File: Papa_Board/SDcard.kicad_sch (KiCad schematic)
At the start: 12 parts, among them J8 693072010801, Q1 BSS138

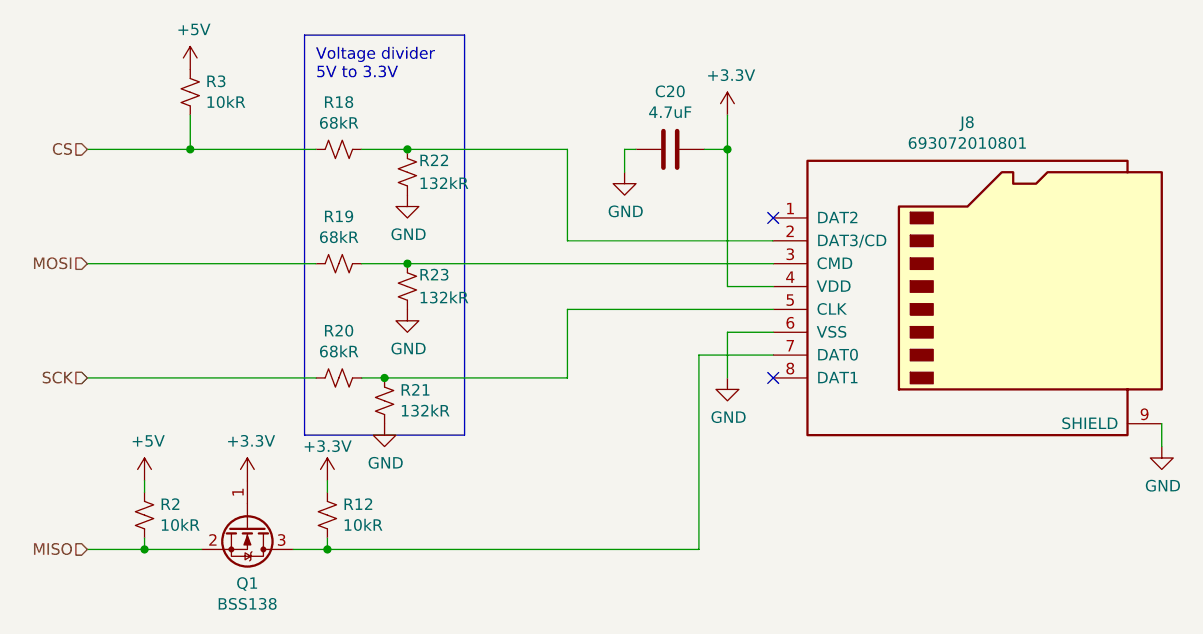
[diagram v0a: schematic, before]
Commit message: Remove level shifting + voltage dividers from SD card SPI lines
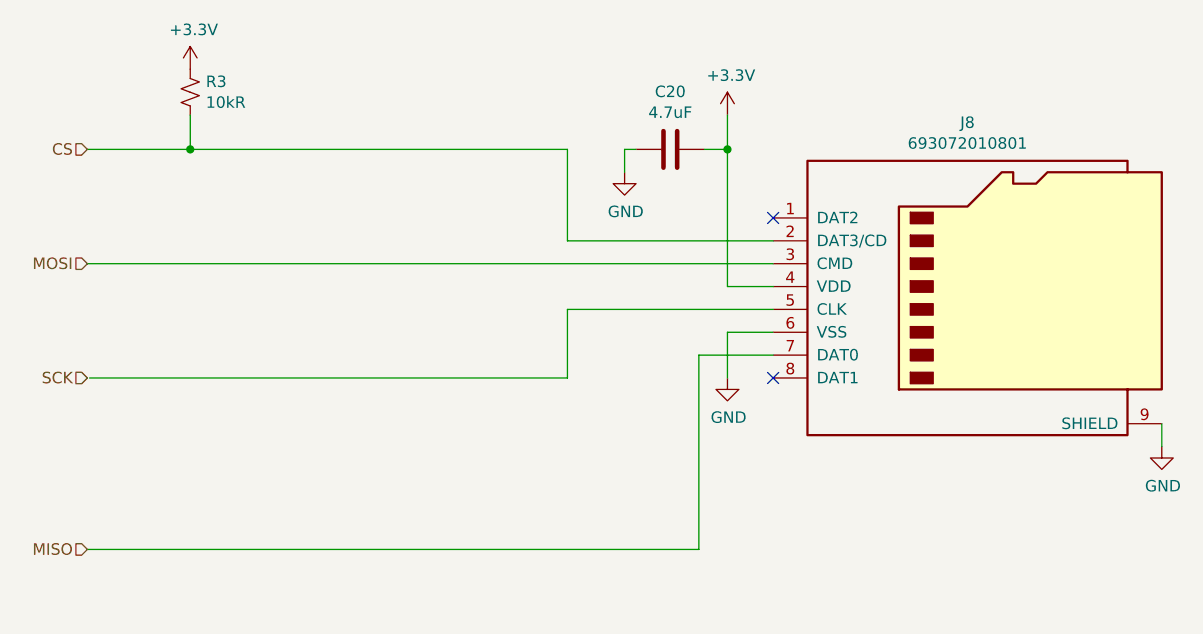
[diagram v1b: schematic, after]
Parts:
- removed Q1: BSS138, Package_TO_SOT_SMD:SOT-23, symbol Device:Q_NMOS_GSD
- removed R12, R2: 10kR, Resistor_SMD:R_0805_2012Metric_Pad1.20x1.40mm_HandSolder, symbol Device:R_Small_US
- removed R18: 68kR, Resistor_SMD:R_0805_2012Metric_Pad1.15x1.40mm_HandSolder, symbol Device:R_Small_US
- removed R19, R20: 68kR, Resistor_SMD:R_0805_2012Metric_Pad1.20x1.40mm_HandSolder, symbol Device:R_Small_US
- removed R21, R23: 132kR, Resistor_SMD:R_0805_2012Metric_Pad1.20x1.40mm_HandSolder, symbol Device:R_Small_US
- removed R22: 132kR, Resistor_SMD:R_0805_2012Metric_Pad1.15x1.40mm_HandSolder, symbol Device:R_Small_US
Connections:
- net +5V is gone; now on net +3V3: R3.1
- net CS: now also J8.2 (DAT3/CD)
- net MISO: now also J8.7 (DAT0)
- net MOSI: now also J8.3 (CMD)
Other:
- note removed: "Voltage divider 5V to 3.3V"

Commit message: Finish changes to PCB layout, clean up and simplify VCC layer
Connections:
- net SCK: now also J8.5 (CLK)
- net CS renamed CS_2
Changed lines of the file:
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@@
     (effects (font (size 1.27 1.27)) (justify right))
   )
-  (hierarchical_label "SCK" (shape input) (at 123.19 107.95 180)
+  (hierarchical_label "SCK" (shape input) (at 123.444 107.95 180)
     (effects (font (size 1.27 1.27)) (justify right))
   )
@@
     (effects (font (size 1.27 1.27)) (justify right))
   )
-  (hierarchical_label "CS" (shape input) (at 123.19 82.55 180)
+  (hierarchical_label "CS_2" (shape input) (at 123.19 82.55 180)
     (effects (font (size 1.27 1.27)) (justify right))
   )
@@
   (symbol (lib_id "power:+3.3V") (at 134.62 73.66 0) (unit 1)
     (in_bom yes) (on_board yes)
-    (property "Reference" "#PWR?" (id 0) (at 134.62 77.47 0)
+    (property "Reference" "#PWR0101" (id 0) (at 134.62 77.47 0)
       (effects (font (size 1.27 1.27)) hide)
     )

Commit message: Minor schematic/pcb adjustments
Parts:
- removed R3: 10kR, Resistor_SMD:R_0805_2012Metric_Pad1.15x1.40mm_HandSolder, symbol Device:R_Small_US
- added R12: 10kR, Resistor_SMD:R_0805_2012Metric_Pad1.20x1.40mm_HandSolder, symbol Device:R_Small_US
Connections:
- net +3V3: now also R12.1
- net CS_2: now also R12.2
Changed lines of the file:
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@@
     (pin "1")
-  )
-  (symbol (lib_id "Device:R_Small_US") (at 134.62 76.2 0) (unit 1)
-    (in_bom yes) (on_board yes)
-    (property "Reference" "R3" (id 0) (at 136.3472 75.0316 0)
-      (effects (font (size 1.27 1.27)) (justify left))
-    )
-    (property "Value" "10kR" (id 1) (at 136.3472 77.343 0)
-      (effects (font (size 1.27 1.27)) (justify left))
-    )
-    (property "Footprint" "Resistor_SMD:R_0805_2012Metric_Pad1.15x1.40mm_HandSolder" (id 2) (at 134.62 76.2 0)
-      (effects (font (size 1.27 1.27)) hide)
-    )
-    (property "Datasheet" "~" (id 3) (at 134.62 76.2 0)
-      (effects (font (size 1.27 1.27)) hide)
-    )
-    (pin "1")
-    (pin "2")
   )
   (symbol (lib_id "power:GND") (at 242.57 115.57 0) (unit 1)
@@
     (pin "1")
   )
+  (symbol (lib_id "Device:R_Small_US") (at 134.62 76.2 0) (unit 1)
+    (in_bom yes) (on_board yes)
+    (property "Reference" "R12" (id 0) (at 136.3472 75.0316 0)
+      (effects (font (size 1.27 1.27)) (justify left))
+    )
+    (property "Value" "10kR" (id 1) (at 136.3472 77.343 0)
+      (effects (font (size 1.27 1.27)) (justify left))
+    )
+    (property "Footprint" "Resistor_SMD:R_0805_2012Metric_Pad1.20x1.40mm_HandSolder" (id 2) (at 134.62 76.2 0)
+      (effects (font (size 1.27 1.27)) hide)
+    )
+    (property "Datasheet" "~" (id 3) (at 134.62 76.2 0)
+      (effects (font (size 1.27 1.27)) hide)
+    )
+    (pin "1")
+    (pin "2")
+  )
 )

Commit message: fixed volgtage logic levels, added test connectors and jumpers
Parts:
- added R21, R22, R23: 10kR, Resistor_SMD:R_0805_2012Metric_Pad1.20x1.40mm_HandSolder, symbol Device:R_Small_US
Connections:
- net +3V3: now also R21.1, R22.1, R23.1
- net MISO: now also R23.2
- net MOSI: now also R21.2
- net SCK: now also R22.2
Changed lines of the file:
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@@
 (kicad_sch (version 20211123) (generator eeschema)
   (paper "A4")
+  (junction (at 135.255 95.25) (diameter 0) (color 0 0 0 0)
+  )
+  (junction (at 135.255 107.95) (diameter 0) (color 0 0 0 0)
+  )
   (junction (at 194.31 82.55) (diameter 0) (color 0 0 0 0)
   )
   (junction (at 134.62 82.55) (diameter 0) (color 0 0 0 0)
+  )
+  (junction (at 135.89 127) (diameter 0) (color 0 0 0 0)
   )
   (no_connect (at 199.39 107.95))
@@
     (stroke (width 0) (type default) (color 0 0 0 0))
   )
-  (wire (pts (xy 123.19 127) (xy 191.135 127))
+  (wire (pts (xy 123.19 127) (xy 135.89 127))
     (stroke (width 0) (type default) (color 0 0 0 0))
   )
@@
     (stroke (width 0) (type default) (color 0 0 0 0))
   )
-  (wire (pts (xy 123.444 107.95) (xy 176.53 107.95))
+  (wire (pts (xy 123.444 107.95) (xy 135.255 107.95))
     (stroke (width 0) (type default) (color 0 0 0 0))
   )
@@
     (stroke (width 0) (type default) (color 0 0 0 0))
   )
+  (wire (pts (xy 135.89 127) (xy 191.135 127))
+    (stroke (width 0) (type default) (color 0 0 0 0))
+  )
   (wire (pts (xy 176.53 100.33) (xy 199.39 100.33))
     (stroke (width 0) (type default) (color 0 0 0 0))
@@
     (stroke (width 0) (type default) (color 0 0 0 0))
   )
+  (wire (pts (xy 135.255 107.95) (xy 176.53 107.95))
+    (stroke (width 0) (type default) (color 0 0 0 0))
+  )
   (wire (pts (xy 182.88 85.09) (xy 182.88 82.55))
     (stroke (width 0) (type default) (color 0 0 0 0))
   )
-  (wire (pts (xy 123.19 95.25) (xy 199.39 95.25))
+  (wire (pts (xy 123.19 95.25) (xy 135.255 95.25))
     (stroke (width 0) (type default) (color 0 0 0 0))
   )
   (wire (pts (xy 194.31 82.55) (xy 194.31 78.74))
+    (stroke (width 0) (type default) (color 0 0 0 0))
+  )
+  (wire (pts (xy 135.255 95.25) (xy 199.39 95.25))
     (stroke (width 0) (type default) (color 0 0 0 0))
   )
@@
     (pin "1")
   )
+  (symbol (lib_id "Device:R_Small_US") (at 135.255 92.71 0) (unit 1)
+    (in_bom yes) (on_board yes)
+    (property "Reference" "R21" (id 0) (at 136.9822 91.5416 0)
+      (effects (font (size 1.27 1.27)) (justify left))
+    )
+    (property "Value" "10kR" (id 1) (at 136.9822 93.853 0)
+      (effects (font (size 1.27 1.27)) (justify left))
+    )
+    (property "Footprint" "Resistor_SMD:R_0805_2012Metric_Pad1.20x1.40mm_HandSolder" (id 2) (at 135.255 92.71 0)
+      (effects (font (size 1.27 1.27)) hide)
+    )
+    (property "Datasheet" "~" (id 3) (at 135.255 92.71 0)
+      (effects (font (size 1.27 1.27)) hide)
+    )
+    (pin "1")
+    (pin "2")
+  )
+  (symbol (lib_id "Device:R_Small_US") (at 135.89 124.46 0) (unit 1)
+    (in_bom yes) (on_board yes)
+    (property "Reference" "R23" (id 0) (at 137.6172 123.2916 0)
+      (effects (font (size 1.27 1.27)) (justify left))
+    )
+    (property "Value" "10kR" (id 1) (at 137.6172 125.603 0)
+      (effects (font (size 1.27 1.27)) (justify left))
+    )
+    (property "Footprint" "Resistor_SMD:R_0805_2012Metric_Pad1.20x1.40mm_HandSolder" (id 2) (at 135.89 124.46 0)
+      (effects (font (size 1.27 1.27)) hide)
+    )
+    (property "Datasheet" "~" (id 3) (at 135.89 124.46 0)
+      (effects (font (size 1.27 1.27)) hide)
+    )
+    (pin "1")
+    (pin "2")
+  )
   (symbol (lib_id "power:+3.3V") (at 134.62 73.66 0) (unit 1)
     (in_bom yes) (on_board yes)
@@
     (pin "1")
   )
+  (symbol (lib_id "power:+3.3V") (at 135.89 121.92 0) (unit 1)
+    (in_bom yes) (on_board yes)
+    (property "Reference" "#PWR025" (id 0) (at 135.89 125.73 0)
+      (effects (font (size 1.27 1.27)) hide)
+    )
+    (property "Value" "+3.3V" (id 1) (at 136.271 117.5258 0))
+    (property "Footprint" "" (id 2) (at 135.89 121.92 0)
+      (effects (font (size 1.27 1.27)) hide)
+    )
+    (property "Datasheet" "" (id 3) (at 135.89 121.92 0)
+      (effects (font (size 1.27 1.27)) hide)
+    )
+    (pin "1")
+  )
+  (symbol (lib_id "power:+3.3V") (at 135.255 90.17 0) (unit 1)
+    (in_bom yes) (on_board yes)
+    (property "Reference" "#PWR022" (id 0) (at 135.255 93.98 0)
+      (effects (font (size 1.27 1.27)) hide)
+    )
+    (property "Value" "+3.3V" (id 1) (at 135.636 85.7758 0))
+    (property "Footprint" "" (id 2) (at 135.255 90.17 0)
+      (effects (font (size 1.27 1.27)) hide)
+    )
+    (property "Datasheet" "" (id 3) (at 135.255 90.17 0)
+      (effects (font (size 1.27 1.27)) hide)
+    )
+    (pin "1")
+  )
+  (symbol (lib_id "Device:R_Small_US") (at 135.255 105.41 0) (unit 1)
+    (in_bom yes) (on_board yes)
+    (property "Reference" "R22" (id 0) (at 136.9822 104.2416 0)
+      (effects (font (size 1.27 1.27)) (justify left))
+    )
+    (property "Value" "10kR" (id 1) (at 136.9822 106.553 0)
+      (effects (font (size 1.27 1.27)) (justify left))
+    )
+    (property "Footprint" "Resistor_SMD:R_0805_2012Metric_Pad1.20x1.40mm_HandSolder" (id 2) (at 135.255 105.41 0)
+      (effects (font (size 1.27 1.27)) hide)
+    )
+    (property "Datasheet" "~" (id 3) (at 135.255 105.41 0)
+      (effects (font (size 1.27 1.27)) hide)
+    )
+    (pin "1")
+    (pin "2")
+  )
   (symbol (lib_id "Device:R_Small_US") (at 134.62 76.2 0) (unit 1)
     (in_bom yes) (on_board yes)
@@
     (pin "2")
   )
+  (symbol (lib_id "power:+3.3V") (at 135.255 102.87 0) (unit 1)
+    (in_bom yes) (on_board yes)
+    (property "Reference" "#PWR024" (id 0) (at 135.255 106.68 0)
+      (effects (font (size 1.27 1.27)) hide)
+    )
+    (property "Value" "+3.3V" (id 1) (at 135.636 98.4758 0))
+    (property "Footprint" "" (id 2) (at 135.255 102.87 0)
+      (effects (font (size 1.27 1.27)) hide)
+    )
+    (property "Datasheet" "" (id 3) (at 135.255 102.87 0)
+      (effects (font (size 1.27 1.27)) hide)
+    )
+    (pin "1")
+  )
 )
